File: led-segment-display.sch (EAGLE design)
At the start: 42 parts

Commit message: led-segment-display : Change to 15 segment display
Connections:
- removed net N$12: LED17.C, LED18.A
- removed net N$4: LED5.C, LED6.A
- removed net N$8: LED11.C, LED12.A
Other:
- moved on the sheet: LED10, LED11, LED12, LED16, LED17, LED18, LED4, LED40, LED41, LED42, LED5, LED6
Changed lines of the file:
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@@
 <instance part="LED2" gate="LED" x="12.7" y="101.6"/>
 <instance part="LED3" gate="LED" x="12.7" y="93.98"/>
-<instance part="LED4" gate="LED" x="22.86" y="116.84" rot="R90"/>
-<instance part="LED5" gate="LED" x="30.48" y="116.84" rot="R90"/>
-<instance part="LED6" gate="LED" x="38.1" y="116.84" rot="R90"/>
+<instance part="LED4" gate="LED" x="15.24" y="116.84" rot="R90"/>
+<instance part="LED5" gate="LED" x="22.86" y="116.84" rot="R90"/>
+<instance part="LED6" gate="LED" x="43.18" y="116.84" rot="R90"/>
 <instance part="LED7" gate="LED" x="53.34" y="109.22"/>
 <instance part="LED8" gate="LED" x="53.34" y="101.6"/>
 <instance part="LED9" gate="LED" x="53.34" y="93.98"/>
-<instance part="LED10" gate="LED" x="22.86" y="83.82" rot="R90"/>
-<instance part="LED11" gate="LED" x="30.48" y="83.82" rot="R90"/>
-<instance part="LED12" gate="LED" x="38.1" y="83.82" rot="R90"/>
+<instance part="LED10" gate="LED" x="15.24" y="83.82" rot="R90"/>
+<instance part="LED11" gate="LED" x="22.86" y="83.82" rot="R90"/>
+<instance part="LED12" gate="LED" x="43.18" y="83.82" rot="R90"/>
 <instance part="LED13" gate="LED" x="12.7" y="76.2"/>
 <instance part="LED14" gate="LED" x="12.7" y="68.58"/>
 <instance part="LED15" gate="LED" x="12.7" y="60.96"/>
-<instance part="LED16" gate="LED" x="22.86" y="48.26" rot="R90"/>
-<instance part="LED17" gate="LED" x="30.48" y="48.26" rot="R90"/>
-<instance part="LED18" gate="LED" x="38.1" y="48.26" rot="R90"/>
+<instance part="LED16" gate="LED" x="15.24" y="48.26" rot="R90"/>
+<instance part="LED17" gate="LED" x="22.86" y="48.26" rot="R90"/>
+<instance part="LED18" gate="LED" x="43.18" y="48.26" rot="R90"/>
 <instance part="LED22" gate="LED" x="33.02" y="109.22"/>
 <instance part="LED23" gate="LED" x="33.02" y="101.6"/>
@@
 <instance part="LED38" gate="LED" x="43.18" y="93.98"/>
 <instance part="LED39" gate="LED" x="43.18" y="60.96"/>
-<instance part="LED40" gate="LED" x="45.72" y="116.84" rot="R90"/>
-<instance part="LED41" gate="LED" x="45.72" y="83.82" rot="R90"/>
-<instance part="LED42" gate="LED" x="45.72" y="48.26" rot="R90"/>
+<instance part="LED40" gate="LED" x="50.8" y="116.84" rot="R90"/>
+<instance part="LED41" gate="LED" x="50.8" y="83.82" rot="R90"/>
+<instance part="LED42" gate="LED" x="50.8" y="48.26" rot="R90"/>
 </instances>
 <busses>
@@
 </segment>
 </net>
-<net name="N$4" class="0">
-<segment>
-<pinref part="LED5" gate="LED" pin="C"/>
-<pinref part="LED6" gate="LED" pin="A"/>
-</segment>
-</net>
 <net name="N$5" class="0">
 <segment>
@@
 <pinref part="LED10" gate="LED" pin="C"/>
 <pinref part="LED11" gate="LED" pin="A"/>
-</segment>
-</net>
-<net name="N$8" class="0">
-<segment>
-<pinref part="LED11" gate="LED" pin="C"/>
-<pinref part="LED12" gate="LED" pin="A"/>
 </segment>
 </net>
@@
 </segment>
 </net>
-<net name="N$12" class="0">
-<segment>
-<pinref part="LED17" gate="LED" pin="C"/>
-<pinref part="LED18" gate="LED" pin="A"/>
-</segment>
-</net>

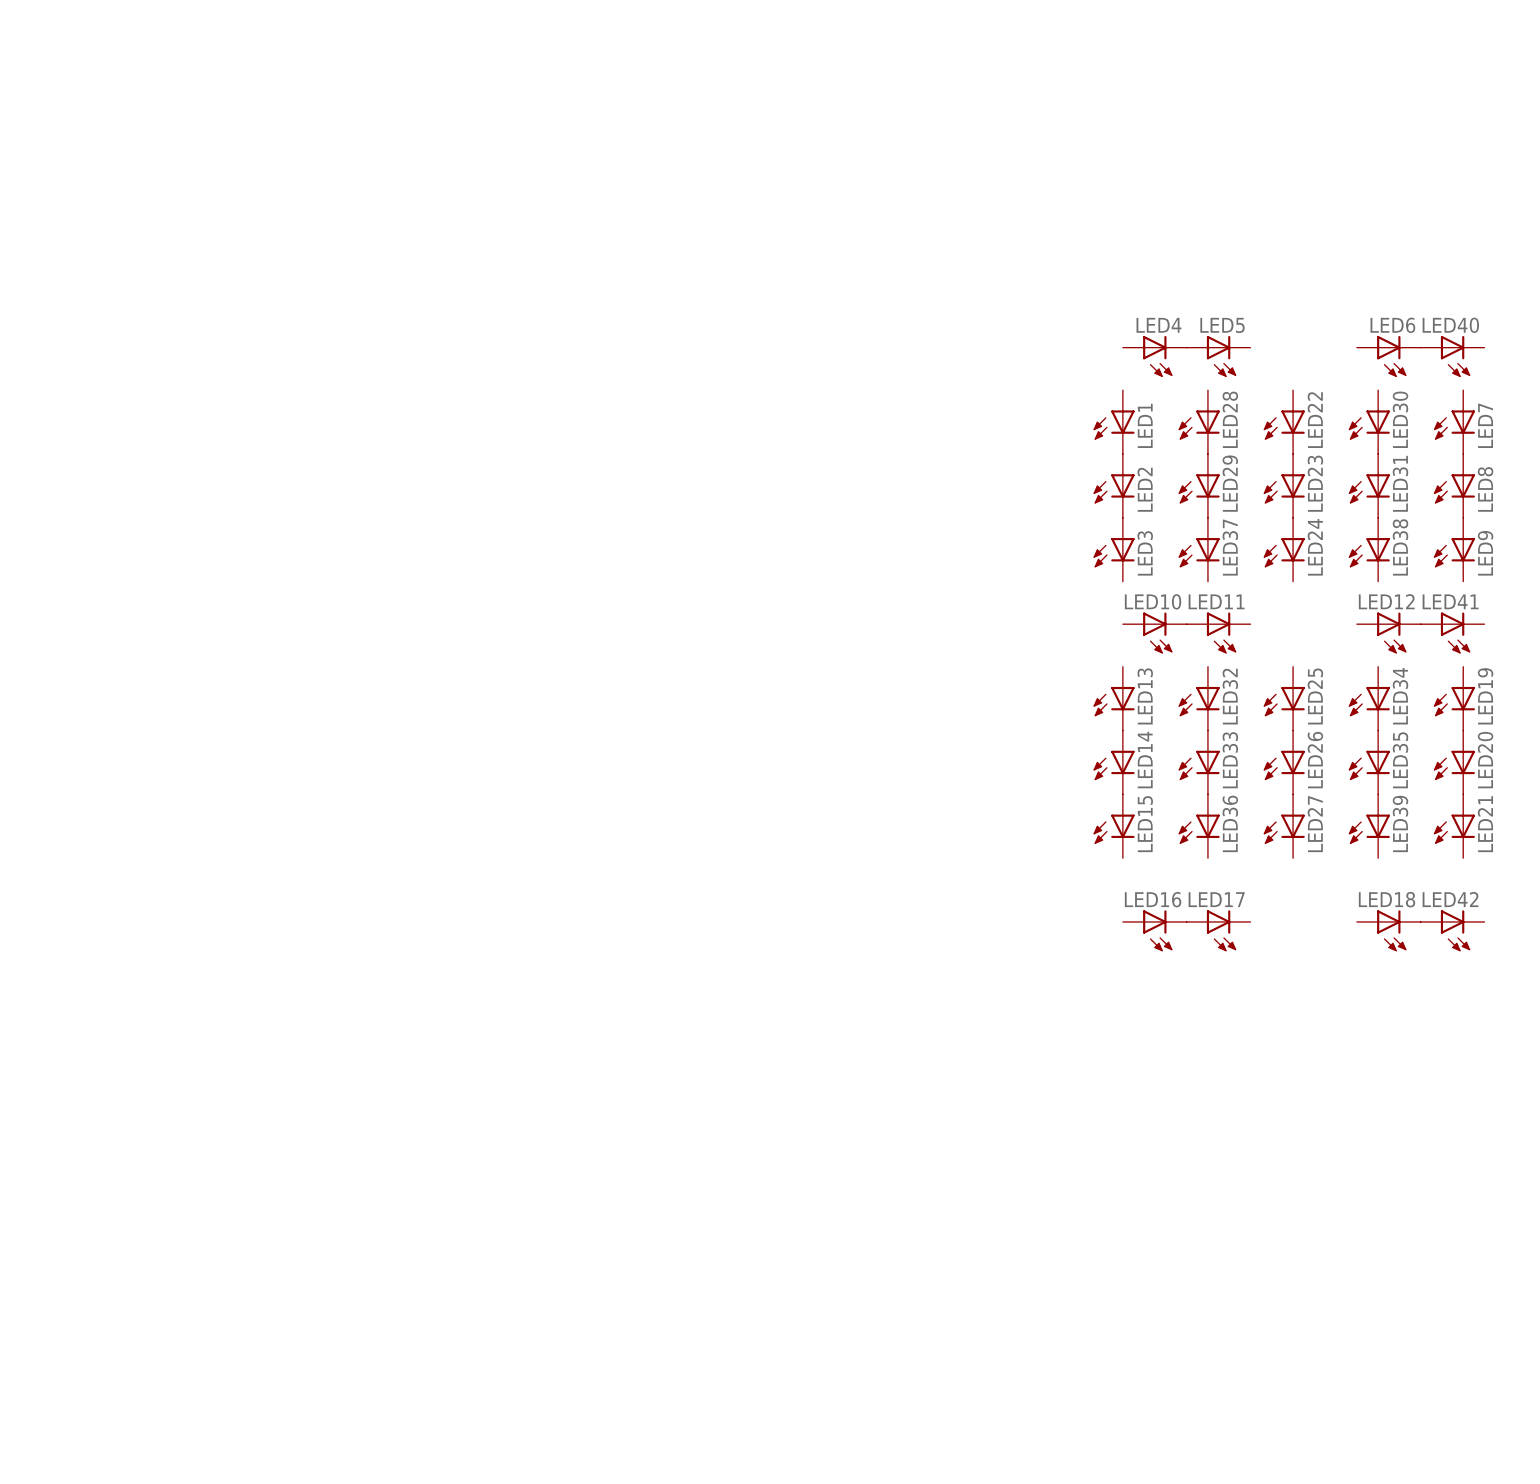
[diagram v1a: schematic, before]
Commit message: led-sgement-display : as sent to oshpark
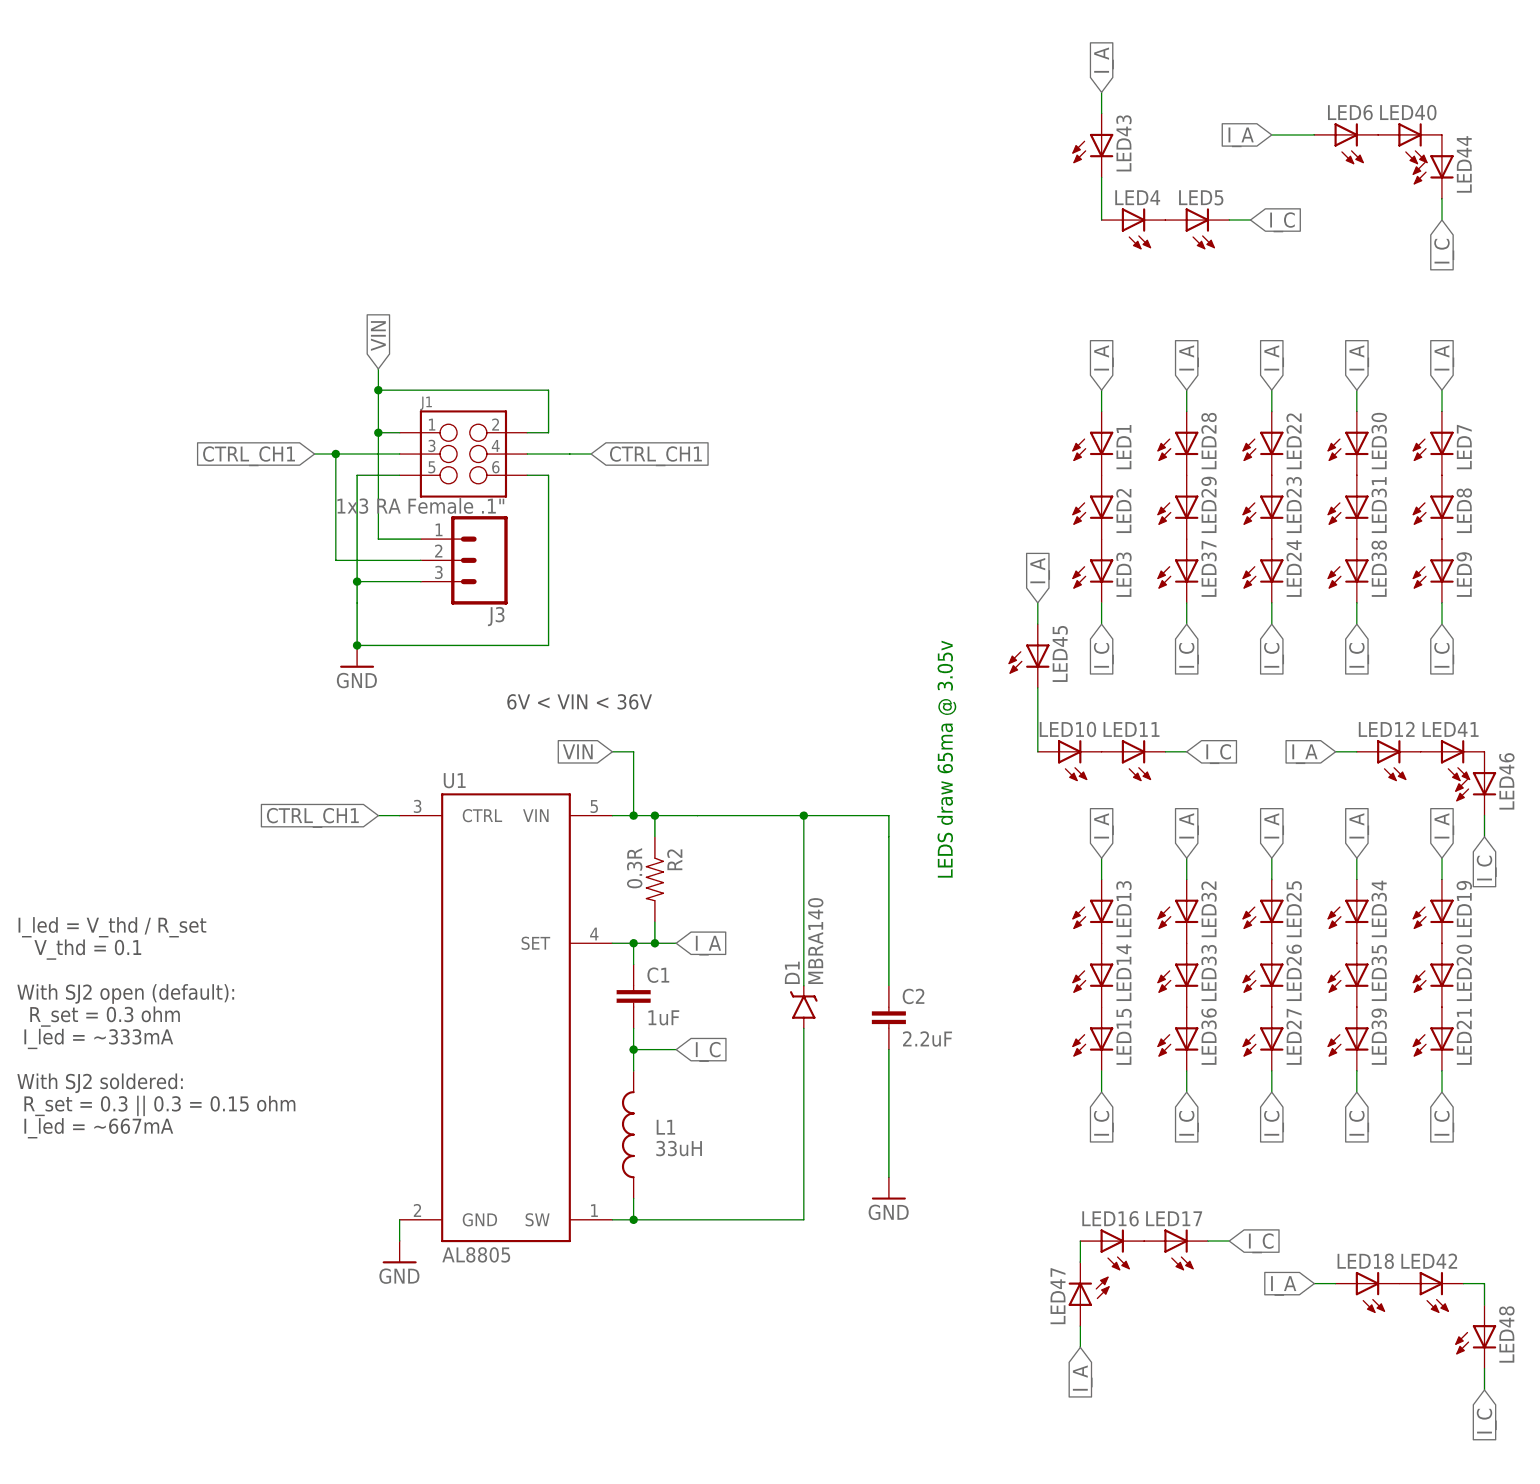
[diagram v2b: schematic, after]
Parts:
- added C1: 1uF, SparkFun-Capacitors:1.0UF50V10%(1206)
- added C2: 2.2uF, SparkFun-Capacitors:2.2UF50V10%(1206)
- added D1: MBRA140, SparkFun-DiscreteSemi:DIODE-SCHOTTKY-MBRA140
- added J1: (no value), mechanical:M03X2SMD
- added J3: 1x3 RA Female .1", mechanical:CONN_03SMD_RA_2.54MM
- added L1: 33uH, SparkFun-Passives:INDUCTORBOURNS_SRN6045
- added LED43, LED44, LED45, LED46, LED47, LED48: (no value), semiconductors:LED3014
- added R2: 0.3R, SparkFun-Resistors:0.3OHM-1/8W-1%(0805)
- added U1: AL8805, SparkFun-PowerIC:AL8805
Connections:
- new net CTRL_CH1: J1.3, J1.4, J3.2, U1.CTRL
- new net GND: C2.2, J1.5, J1.6, J3.3, U1.GND
- new net I_A: C1.1, LED1.A, LED12.A, LED13.A, LED18.A, LED19.A, LED22.A, LED25.A, LED28.A, LED30.A, LED32.A, LED34.A, LED43.A, LED45.A, LED47.A, LED6.A, LED7.A, R2.2, U1.SET
- new net I_C: C1.2, L1.2, LED11.C, LED15.C, LED17.C, LED21.C, LED24.C, LED27.C, LED3.C, LED36.C, LED37.C, LED38.C, LED39.C, LED44.C, LED46.C, LED48.C, LED5.C, LED9.C
- new net N$12: LED42.C, LED48.A
- new net N$34: LED16.A, LED47.C
- new net N$35: LED10.A, LED45.C
- new net N$36: LED41.C, LED46.A
- new net N$4: LED4.A, LED43.C
- new net N$8: LED40.C, LED44.A
- new net SW: D1.A, L1.1, U1.SW
- new net VIN: C2.1, D1.C, J1.1, J1.2, J3.1, R2.1, U1.VIN
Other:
- note added: "6V < VIN < 36V"
- note added: "I_led = V_thd / R_set V_thd = 0.1 With SJ2 open (default): R_set = 0.3 ohm I_led = ~333mA With SJ2 soldered: R_set = 0.3 || 0.3 = 0.15 ohm I_led = ~667mA"
- note added: "LEDS draw 65ma @ 3.05v"
- moved on the sheet: LED1, LED10, LED11, LED12, LED13, LED14, LED15, LED16, LED17, LED18, LED19, LED2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
